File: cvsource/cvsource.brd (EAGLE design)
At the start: 101.6 x 216.8 mm, 101 parts, among them IC1 OPA4130P, IC2 OPA2134P, IC3 78L05Z, J1 UBBS-4R-D14-4D, P1 US-EVUF3J, P2 US-EVUF3J, P3 US-EVUF3J, P4 US-EVUF3J, X1 2516-

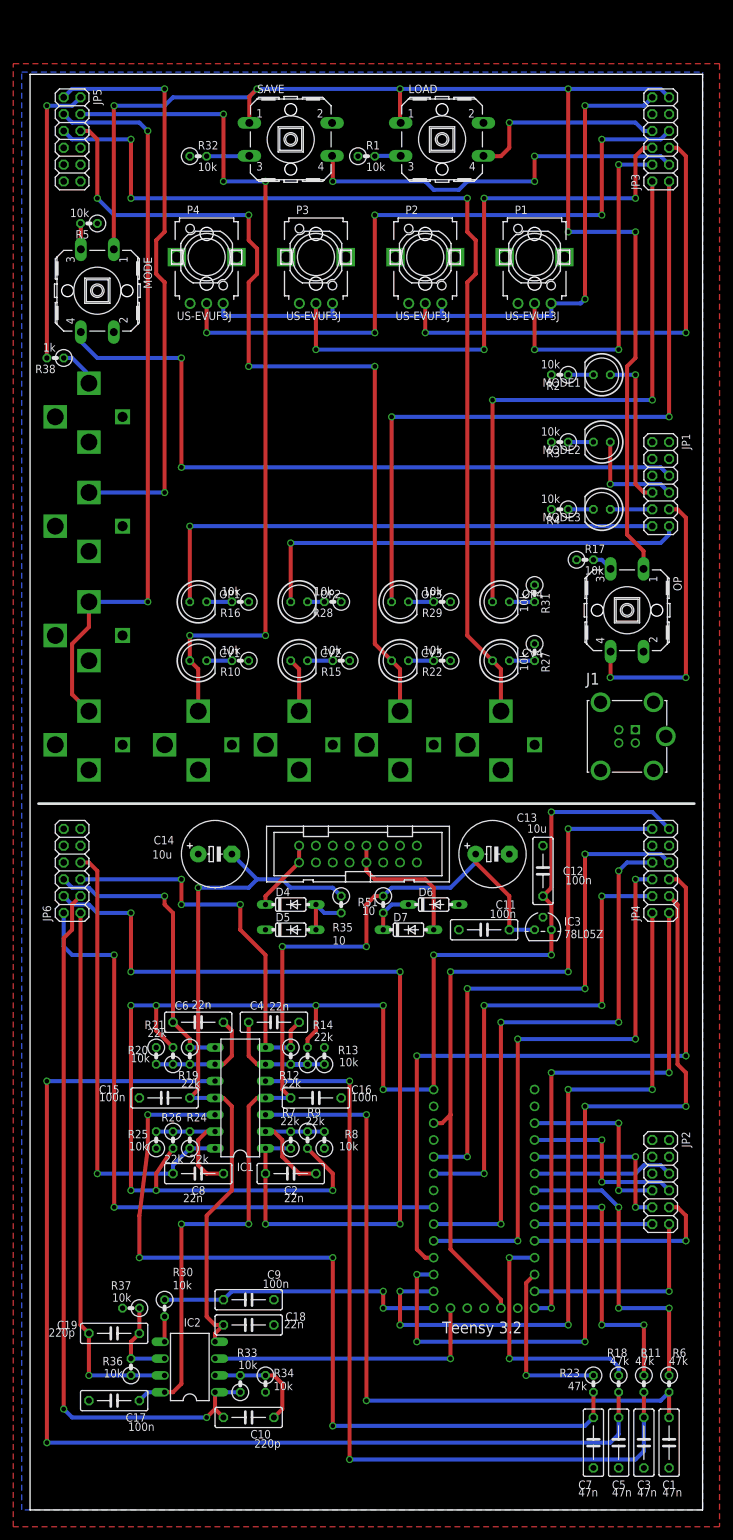
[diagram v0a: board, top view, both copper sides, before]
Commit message: cleaned up cvsource board, flipped power connector
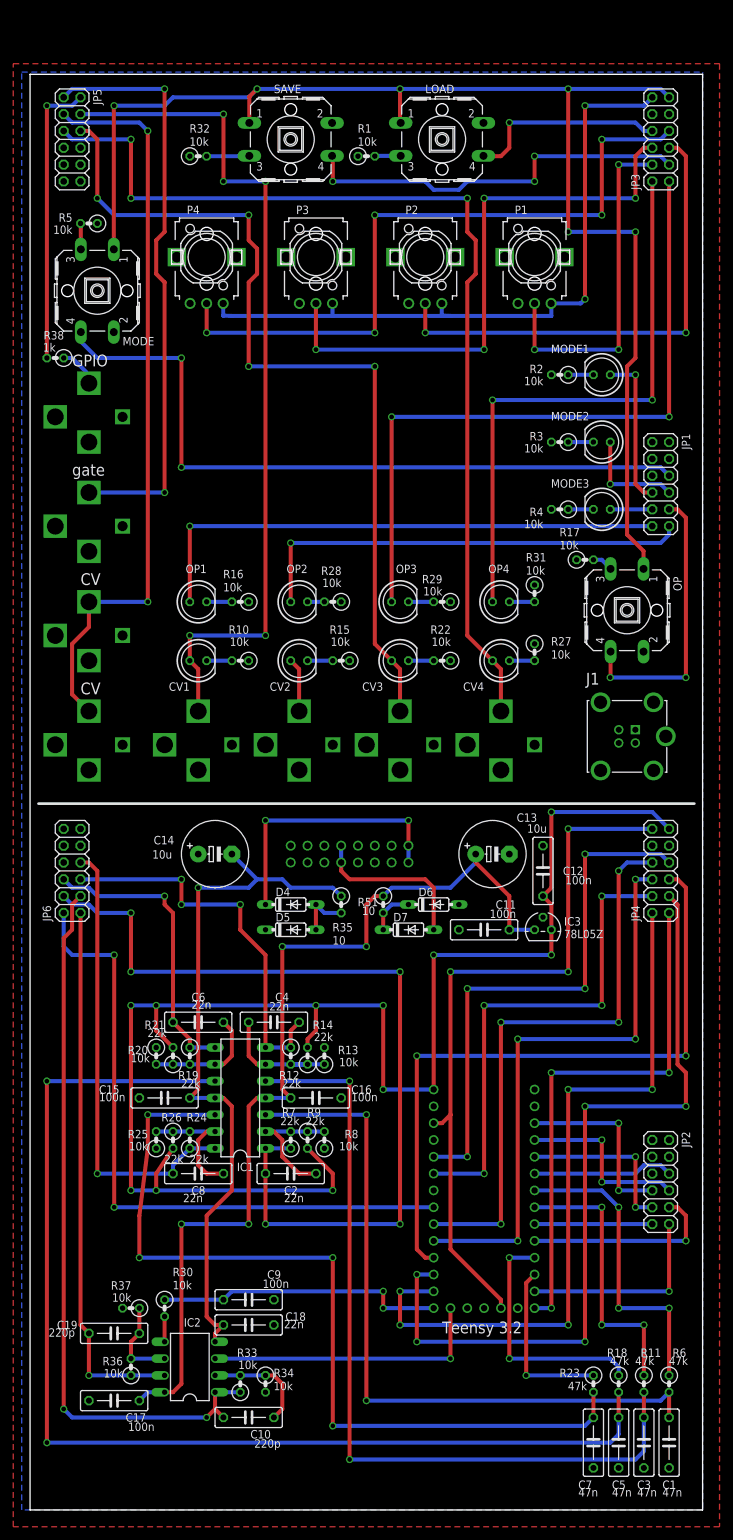
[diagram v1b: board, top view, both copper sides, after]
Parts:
- moved X1 1.27 mm to (48.3, 99.1), flipped to the bottom
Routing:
- net N$72: track 11.0 -> 40.6 mm, vias 0 -> 2
- net N$71: track 21.4 -> 25.2 mm
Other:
- board text added: "-12V"
- board text added: "CV"
- board text added: "GPIO"
- board text added: "gate"

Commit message: added usb and moved things on cvsource
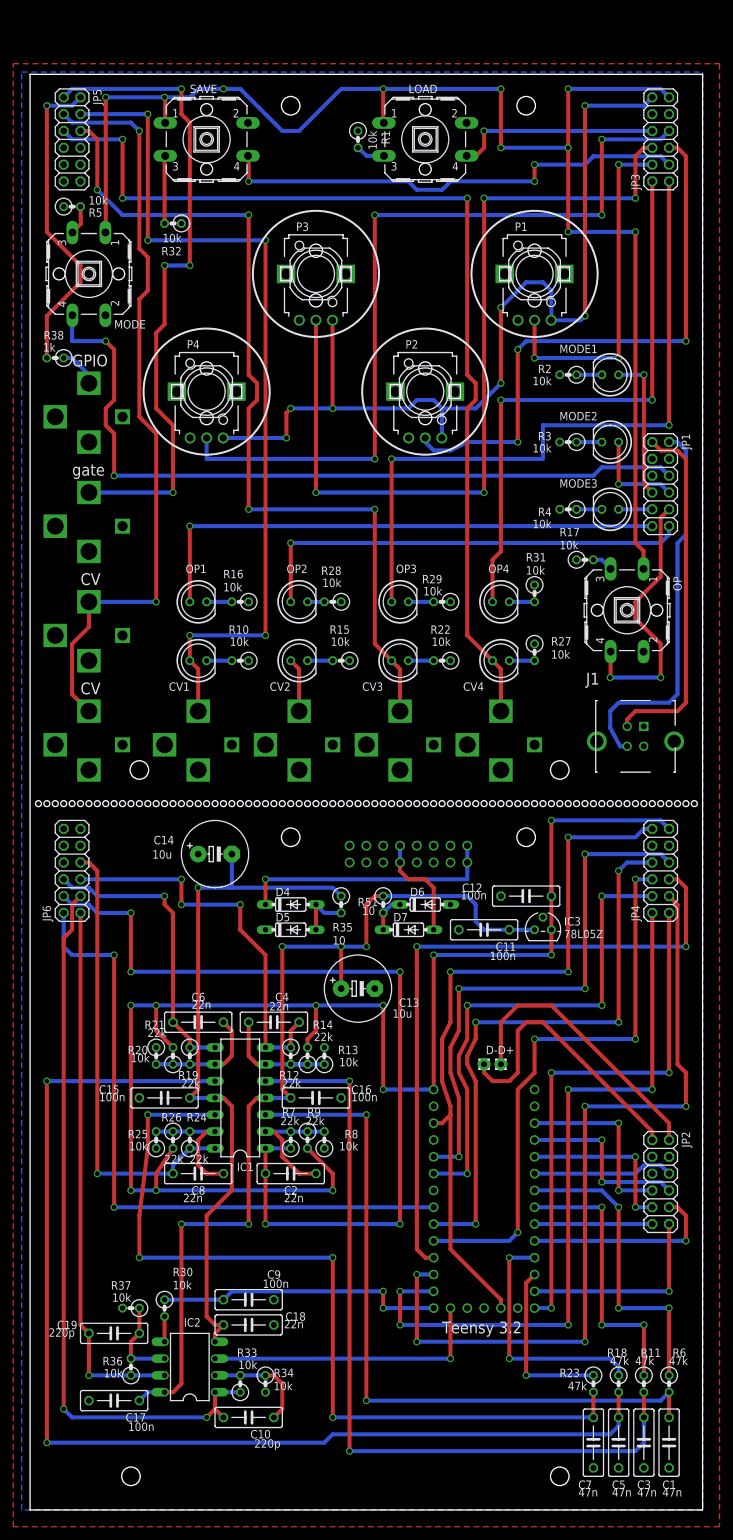
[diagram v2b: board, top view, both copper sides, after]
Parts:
- added D+, D-: (no value), synthdiy:2,0/0,9-R
- moved C13 28.7 mm to (49.5, 78.7)
- moved P2 20.3 mm to (59.7, 168.9)
- moved P4 20.3 mm to (26.7, 168.9)
- moved SAVE 12.7 mm to (26.7, 207.0)
- moved R32 10.9 mm to (21.6, 194.3), turned to 180 degrees
- moved X1 8.89 mm to (57.1, 99.1)
- moved C12 4.58 mm to (74.9, 92.7), turned to 180 degrees
- moved R5 3.59 mm to (6.35, 196.8), turned to 0 degrees
- moved MODE 2.84 mm to (8.89, 186.7)
- moved R1 2.84 mm to (49.5, 207.0), turned to 270 degrees
- moved LOAD 2.54 mm to (59.7, 207.0)
- moved P1 2.54 mm to (76.2, 186.7)
- moved P3 2.54 mm to (43.2, 186.7)
- moved D6 1.27 mm to (59.7, 91.4)
- moved J1 1.27 mm to (91.4, 116.8)
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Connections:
- new net D+A: D+.1, JP2.2
- new net D+B: J1.D+, JP1.2
- new net D-A: D-.1, JP2.1
- new net D-B: J1.D-, JP1.1
- net GND: now also J1.GND, J1.SH1, J1.SH5; no longer JP1.1, JP1.2, JP2.1, JP2.2
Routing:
- net D+B: track 0.00 -> 58.4 mm
- net D-B: track 0.00 -> 53.9 mm
- net D-A: track 0.00 -> 42.7 mm
- net D+A: track 0.00 -> 42.7 mm
- net P3B: track 87.5 -> 128.1 mm
- net 3.3VB: track 103.7 -> 140.0 mm, vias 2 -> 7
- net P4B: track 104.0 -> 121.8 mm, vias 5 -> 4
- net P2B: track 73.5 -> 86.3 mm, vias 2 -> 3
- net SAVEB: track 60.1 -> 72.0 mm
- net 5VB: track 202.2 -> 213.1 mm, vias 6 -> 10
- net N$71: track 25.2 -> 16.3 mm
- net GATEB: track 89.2 -> 97.9 mm, vias 2 -> 4
- net MODEB: track 108.4 -> 115.8 mm
- net GPIO1B: track 43.7 -> 47.9 mm
- net N$37: track 6.47 -> 10.3 mm
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
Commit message: moved things around on cvsource
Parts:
- removed J1: UBBS-4R-D14-4D, UBBS-4R-D14-4D:JST_UBBS-4R-D14-4D
- added GATE: (no value), dan:LED5MM
- added R39: 10k, dan:0207/2V
- added USB: UBBS-4R-D14-4D, UBBS-4R-D14-4D:JST_UBBS-4R-D14-4D
- moved R5 83.8 mm to (90.2, 195.6), turned to 180 degrees
- moved MODE 78.8 mm to (87.6, 185.4)
- moved CVOUT7 22.9 mm to (8.89, 188.0)
- moved R38 22.9 mm to (3.81, 196.8)
- moved C17 11.5 mm to (24.1, 17.8), turned to 0 degrees
- moved R1 10.5 mm to (39.4, 204.5), turned to 0 degrees
- moved LOAD 8.89 mm to (50.8, 207.0)
- moved P1 7.73 mm to (68.6, 188.0)
- moved P2 6.48 mm to (53.3, 170.2)
- moved P3 5.24 mm to (38.1, 188.0)
- moved R17 5.24 mm to (78.7, 142.2), turned to 90 degrees
- moved C10 4.58 mm to (35.6, 17.8)
- moved C9 3.81 mm to (33.0, 35.6)
- moved MODE3 3.81 mm to (87.6, 154.9)
- moved C18 3.81 mm to (33.0, 31.8)
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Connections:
- new net N$6: GATE.K, R39.2
- net D+B: now also USB.D+; no longer J1.D+
- net D-B: now also USB.D-; no longer J1.D-
- net GATEB: now also GATE.A
- net GND: now also R39.1, USB.GND, USB.SH1, USB.SH5; no longer J1.GND, J1.SH1, J1.SH5
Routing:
- net MODEB: track 115.8 -> 34.0 mm, vias 2 -> 1
- net 5VB: track 213.1 -> 177.9 mm, vias 10 -> 6
- net GPIO1B: track 47.9 -> 20.8 mm
- net CVB: track 114.5 -> 134.5 mm, vias 2 -> 6
- net OPB: track 40.6 -> 25.0 mm, vias 2 -> 0
- net CV1B: track 130.1 -> 115.9 mm
- net P2B: track 86.3 -> 98.9 mm, vias 3 -> 4
- net P4B: track 121.8 -> 130.7 mm, vias 4 -> 5
- net LOADB: track 31.1 -> 40.0 mm
- net 3.3VB: track 140.0 -> 131.2 mm, vias 7 -> 6
- net P1B: track 52.7 -> 60.1 mm
- net CVA: track 110.6 -> 117.1 mm
- net N$20: track 3.19 -> 8.84 mm
- net N$6: track 0.00 -> 5.08 mm
- net +12V: track 144.7 -> 140.3 mm
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
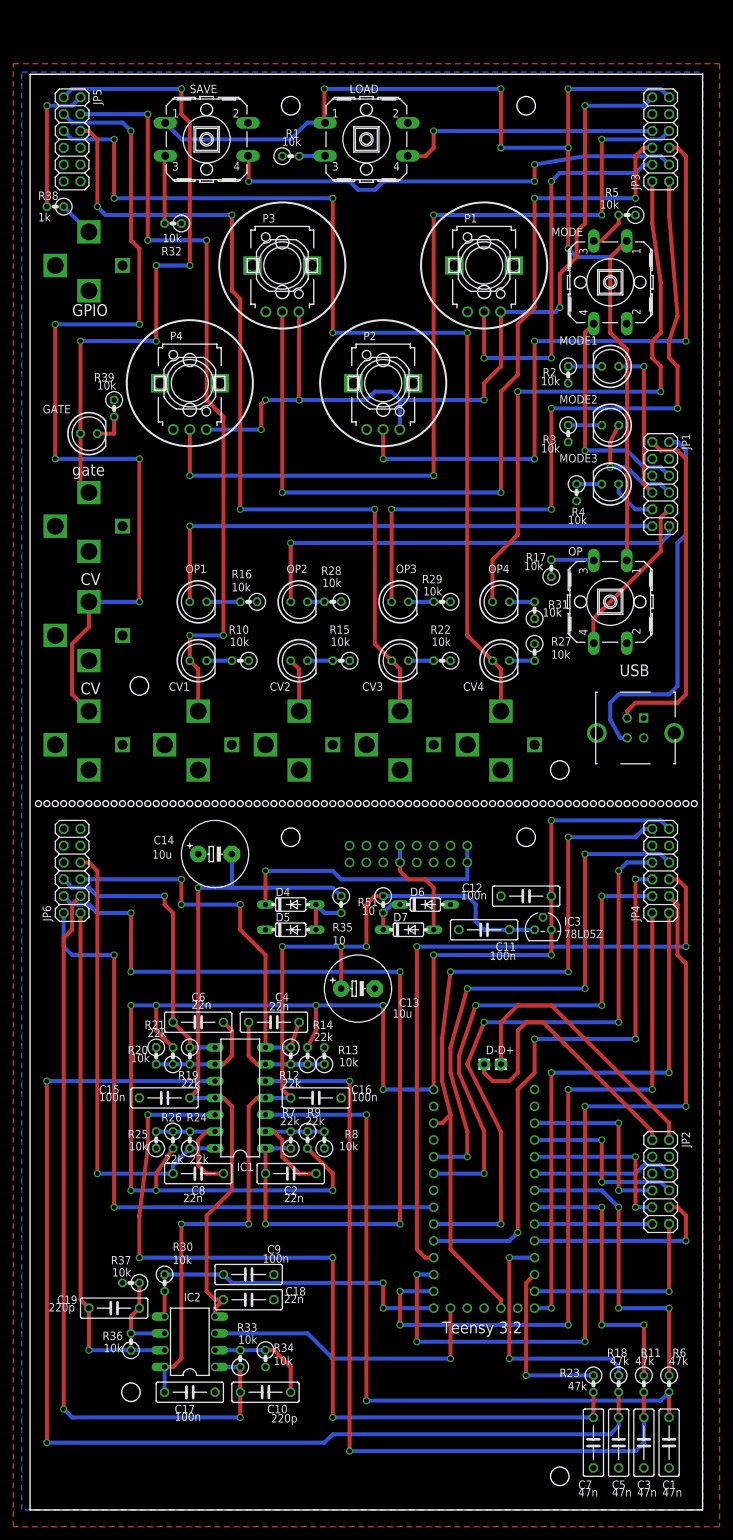
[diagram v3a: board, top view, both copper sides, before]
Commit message: more work on cvsource and added zipped code
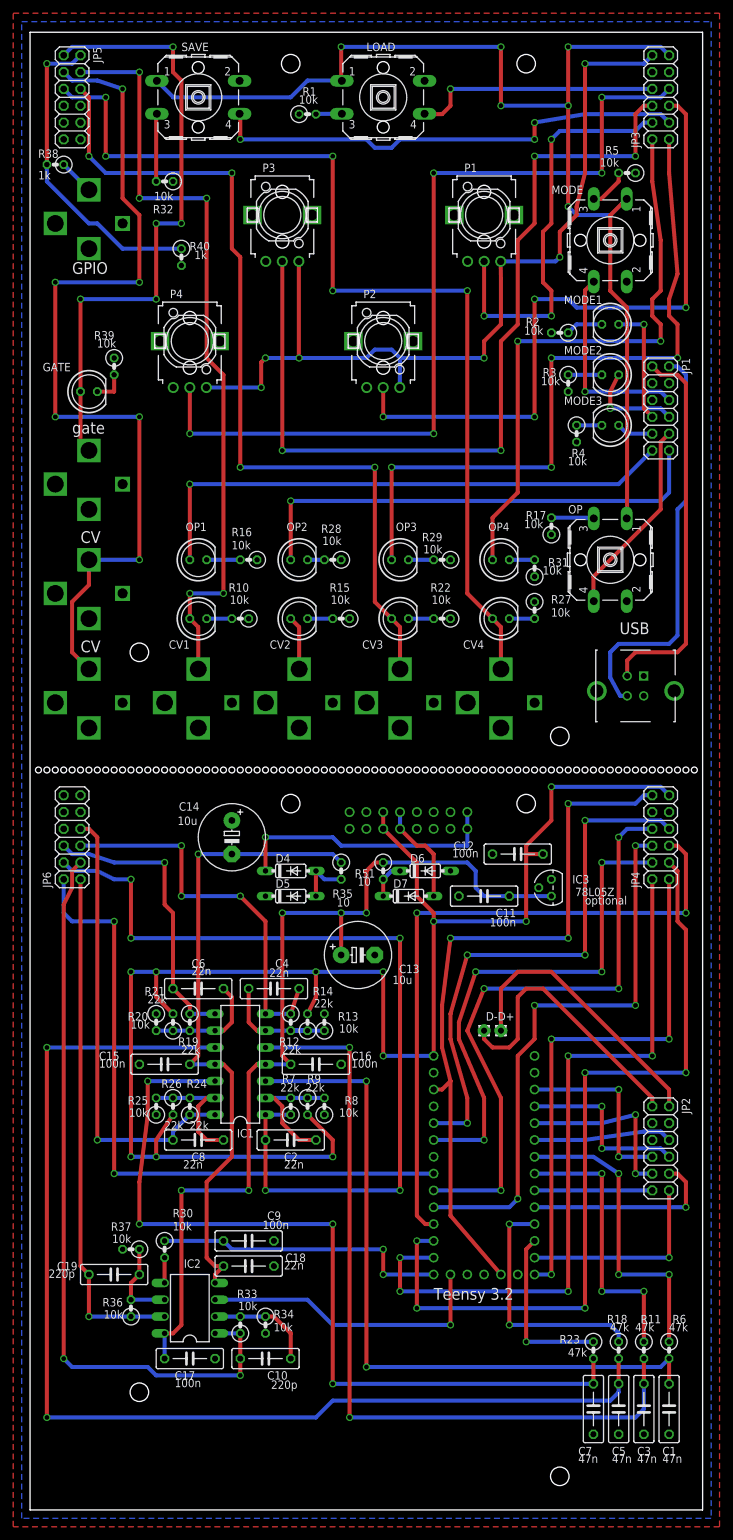
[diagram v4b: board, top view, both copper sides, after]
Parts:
- added R40: 1k, dan:0207/2V
- moved JP1 11.4 mm to (95.2, 166.4)
- moved MODE3 8.89 mm to (87.6, 163.8)
- moved R4 8.89 mm to (82.5, 162.6)
- moved P1 7.62 mm to (68.6, 195.6)
- moved P3 7.62 mm to (38.1, 195.6)
- moved R3 7.62 mm to (81.3, 170.2)
- moved MODE2 7.62 mm to (87.6, 171.4)
- moved LOAD 6.84 mm to (53.3, 213.4)
- moved R1 6.84 mm to (41.9, 210.8)
- moved SAVE 6.48 mm to (25.4, 213.4)
- moved R2 6.48 mm to (80.0, 177.8), turned to 180 degrees
- moved C12 6.48 mm to (73.7, 99.1)
- moved IC3 6.48 mm to (78.7, 94.0), turned to 90 degrees
- moved R32 6.48 mm to (20.3, 200.7)
- moved JP3 6.35 mm to (95.2, 213.4)
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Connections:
- net 5V: now also X1.11, X1.12; no longer IC3.1
- net GND: now also R40.2
- net GPIO1B: now also R40.1
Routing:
- net GPIO1B: track 20.8 -> 47.9 mm
- net 5V: track 223.9 -> 242.6 mm
- net OP2B: track 67.8 -> 72.9 mm
- net MODE1B: track 23.4 -> 18.3 mm
- net -12V: track 102.0 -> 96.9 mm
- net OPB: track 25.0 -> 30.1 mm
- net D-B: track 52.7 -> 57.7 mm
- net D+B: track 57.1 -> 62.2 mm
- net MODEB: track 34.0 -> 30.4 mm
- net CVA: track 117.1 -> 113.6 mm
- net +12V: track 140.3 -> 142.9 mm
- net GATEB: track 96.8 -> 94.3 mm
- net LOADB: track 40.0 -> 37.5 mm
- net MODE2B: track 17.1 -> 14.8 mm
- net P1B: track 60.1 -> 62.4 mm
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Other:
- board size 101.6 x 216.8 mm -> 101.6 x 223.2 mm
- board text added: "A"
- board text added: "D"
- board text added: "LFO"
- board text added: "R"
- board text added: "S"
- board text added: "env"
- board text added: "freq"
- board text added: "kb"
- board text added: "optional"
- board text added: "os"
- board text added: "sync"
- board text added: "vel"
- board text added: "wave"

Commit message: added tri and linear mod to vco, fixed serious errors with cvsource
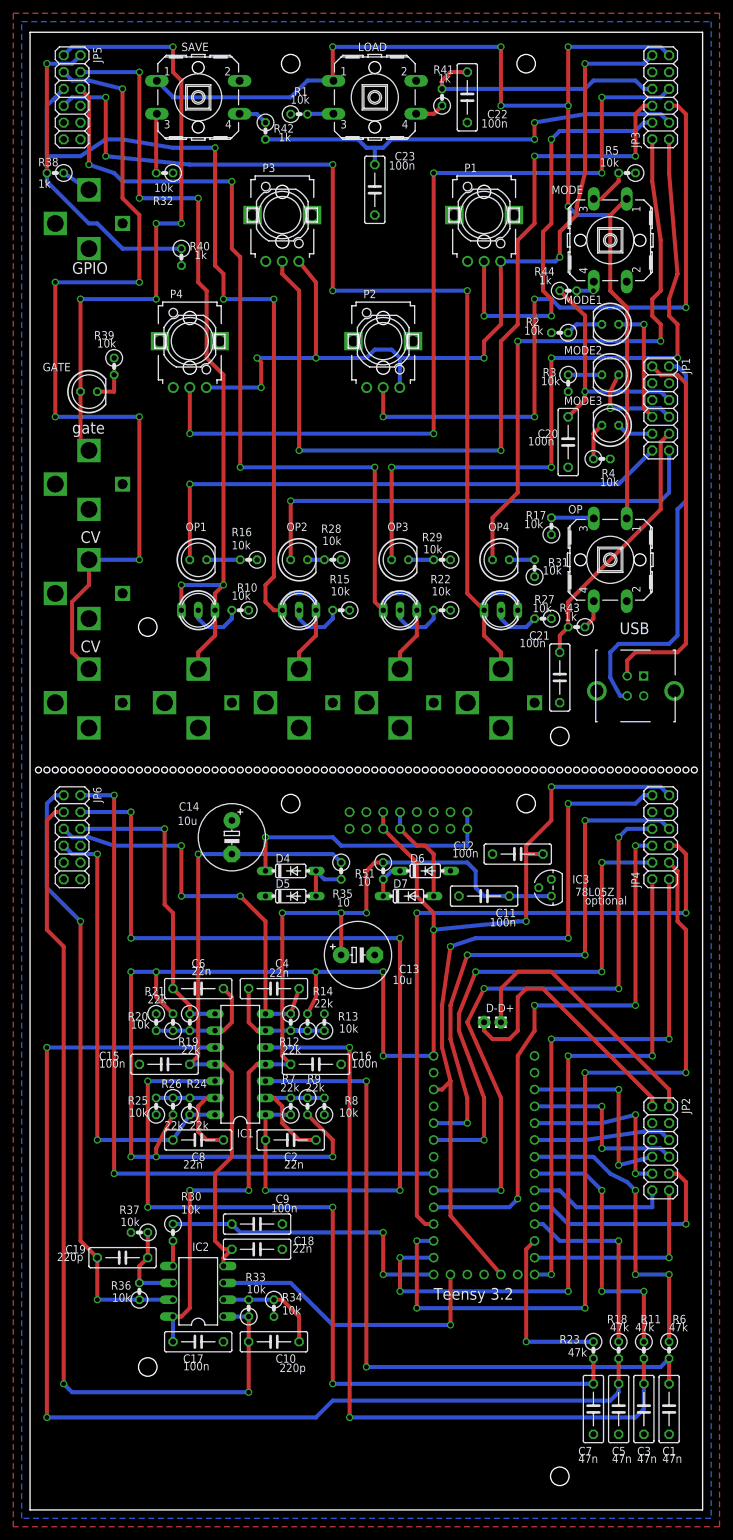
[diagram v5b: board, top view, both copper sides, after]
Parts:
- removed CV1, CV2, CV3, CV4: (no value), dan:LED5MM
- added C20, C21, C22, C23: 100n, dan:C075-032X103
- added D1, D2, D3, D8: (no value), dan:DUOLED5MM
- added R41, R42, R43, R44: 1k, dan:0207/2V
- moved R4 5.39 mm to (86.4, 158.8), turned to 0 degrees
- moved R36 2.84 mm to (16.5, 33.0)
- moved IC2 2.84 mm to (25.4, 33.0)
- moved R33 2.84 mm to (33.0, 30.5)
- moved C19 2.84 mm to (14.0, 38.1)
- moved R37 2.84 mm to (16.5, 41.9)
- moved C17 2.84 mm to (25.4, 25.4)
- moved R30 2.84 mm to (21.6, 41.9)
- moved C10 2.84 mm to (36.8, 25.4)
- moved C18 2.84 mm to (34.3, 39.4)
- moved C9 2.84 mm to (34.3, 43.2)
- moved R34 2.84 mm to (36.8, 30.5)
- moved R27 1.80 mm to (77.5, 134.6), turned to 180 degrees
- moved R32 1.27 mm to (20.3, 201.9)
- moved LOAD 1.27 mm to (52.1, 213.4)
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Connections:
- removed net N$29: CV4.K, R27.2
- new net N$12: R42.1, SAVE.4
- new net N$16: OP.4, R43.1
- new net N$18: MODE.4, R44.2
- new net N$19: D1.K, R27.2
- new net N$7: LOAD.4, R41.1
- net CV1B: now also D8.AG, D8.AR; no longer CV1.A
- net CV2B: now also D3.AG, D3.AR, JP5.5; no longer CV2.A
- net CV3B: now also D2.AG, D2.AR; no longer CV3.A
- net CV4B: now also D1.AG, D1.AR, JP5.7; no longer CV4.A, JP5.5
- net GND: now also C20.2, C21.2, C22.1, C23.1; no longer JP5.7
- net LOADB: now also C22.2, R41.2; no longer LOAD.4
- net MODEB: now also C20.1, R44.1; no longer MODE.4
- net N$13: now also D8.K; no longer CV1.K
- net N$17: now also D3.K; no longer CV2.K
- net N$24: now also D2.K; no longer CV3.K
- net OPB: now also C21.1, R43.2; no longer OP.4
- net SAVEB: now also C23.2, R42.2; no longer SAVE.4
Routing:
- net CV2B: track 8.15 -> 136.4 mm, vias 0 -> 3
- net CVA: track 113.6 -> 132.9 mm
- net GATEA: track 78.0 -> 92.6 mm, vias 1 -> 2
- net GPIO1A: track 99.6 -> 110.5 mm
- net OPB: track 30.1 -> 39.9 mm
- net N$21: track 37.4 -> 29.0 mm, vias 2 -> 1
- net CV3B: track 130.7 -> 139.0 mm
- net CV4B: track 150.0 -> 157.4 mm
- net N$19: track 0.00 -> 7.40 mm
- net CV1A: track 134.2 -> 141.0 mm
- net CV1B: track 115.9 -> 121.3 mm
- net SAVEB: track 72.9 -> 67.7 mm, vias 3 -> 2
- net N$13: track 3.81 -> 8.67 mm
- net N$17: track 3.81 -> 8.67 mm
- net N$24: track 3.81 -> 8.67 mm
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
